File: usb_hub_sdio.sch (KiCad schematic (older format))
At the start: 26 parts, among them Q901 DMG2301L, U901 MA8627, Y901 24MHz

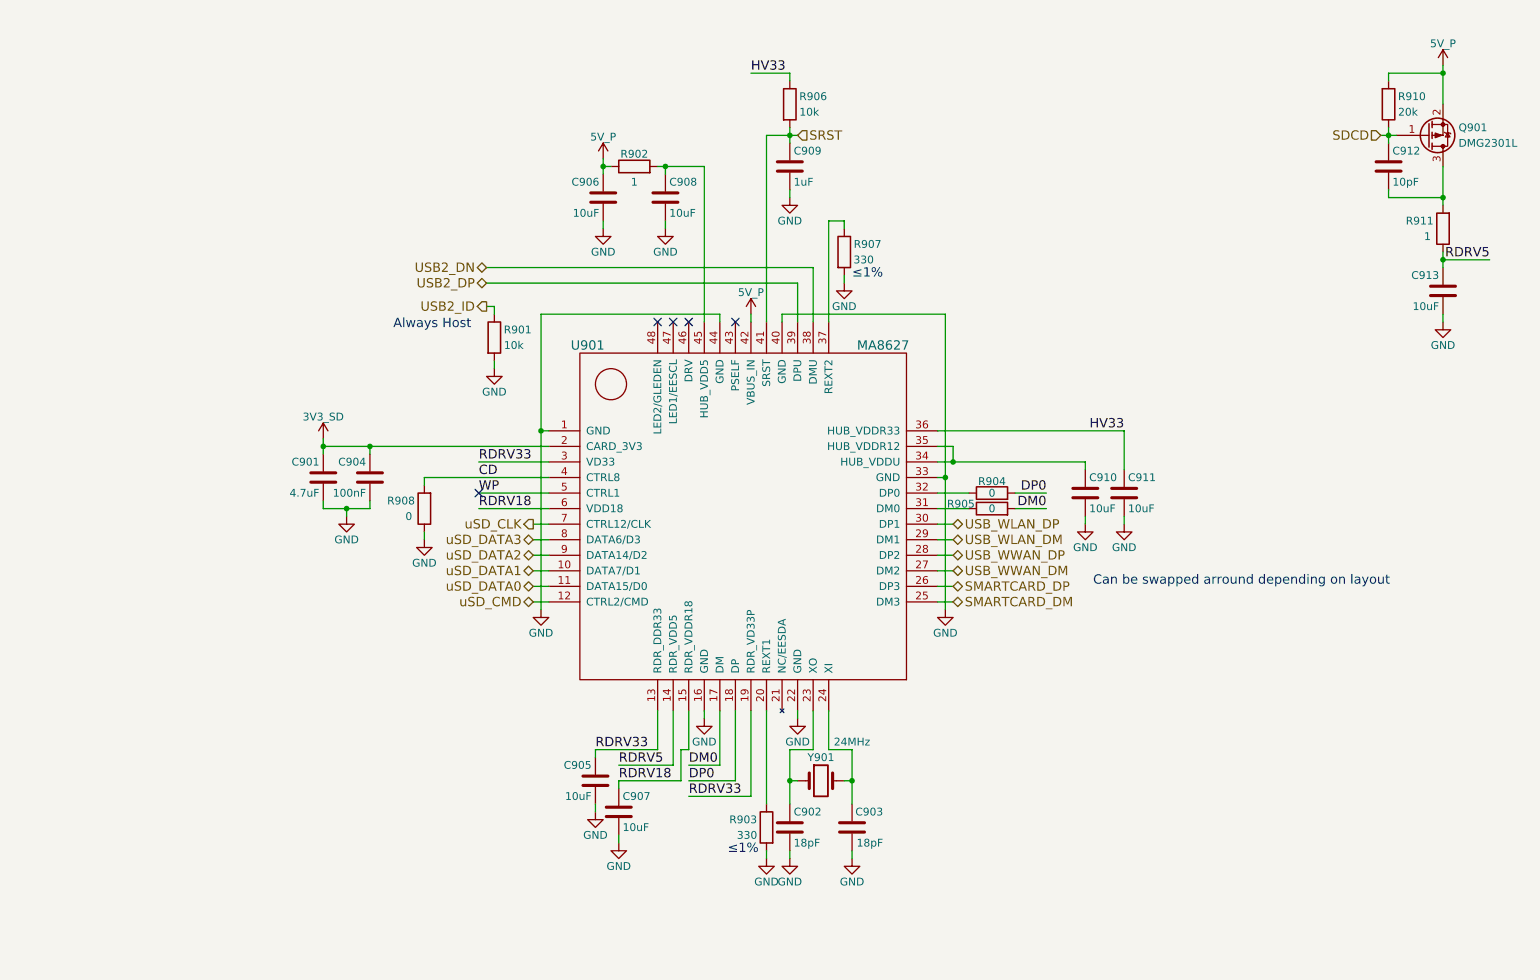
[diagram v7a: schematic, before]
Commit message: Modify the boot config/boot mode pins and switch such that only eMMC and USB (serial downloader) are boot options due to the uSD being attached to the USB<->SD bridge chip, add OV5460 notes about using the internal DVDD 1.5V regulator
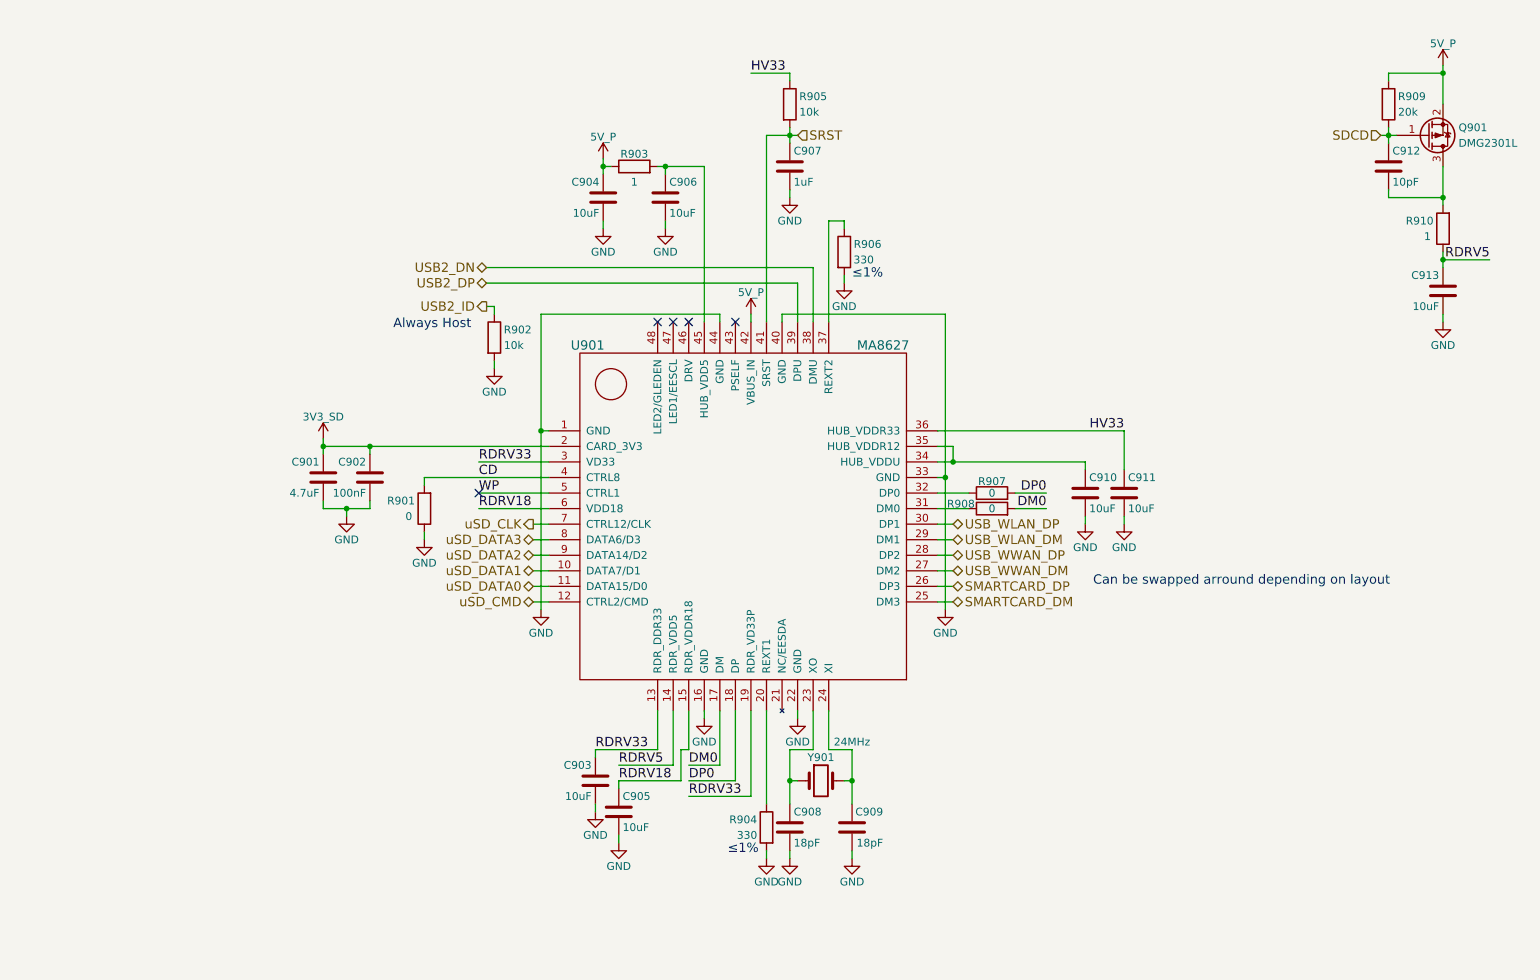
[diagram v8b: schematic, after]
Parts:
- renumbered C904 to C902, C905 to C903, C906 to C904, C907 to C905, C908 to C906, C909 to C907, C902 to C908, C903 to C909, R908 to R901, R901 to R902, R902 to R903, R903 to R904, R906 to R905, R907 to R906, R904 to R907, R905 to R908, R910 to R909, R911 to R910
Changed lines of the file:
@@
 $EndDescr
 $Comp
-L GND #PWR0138
+L GND #PWR0132
 U 1 1 5AFD409A
 P 6100 6050
-F 0 "#PWR0138" H 6100 5800 50  0001 C CNN
+F 0 "#PWR0132" H 6100 5800 50  0001 C CNN
 F 1 "GND" H 6100 5900 50  0000 C CNN
 F 2 "" H 6100 6050 50  0001 C CNN
@@
 $EndComp
 $Comp
-L GND #PWR0139
+L GND #PWR0133
 U 1 1 5AFD422F
 P 6500 6050
-F 0 "#PWR0139" H 6500 5800 50  0001 C CNN
+F 0 "#PWR0133" H 6500 5800 50  0001 C CNN
 F 1 "GND" H 6500 5900 50  0000 C CNN
 F 2 "" H 6500 6050 50  0001 C CNN
@@
 $EndComp
 $Comp
-L C C902
+L C C908
 U 1 1 5AFD532B
 P 6100 5850
-F 0 "C902" H 6125 5750 50  0000 L CNN
+F 0 "C908" H 6125 5750 50  0000 L CNN
 F 1 "18pF" H 6125 5950 50  0000 L CNN
 F 2 "Capacitors_SMD:C_0603" H 6138 5700 50  0001 C CNN
@@
 $EndComp
 $Comp
-L C C903
+L C C909
 U 1 1 5AFD53BF
 P 6500 5850
-F 0 "C903" H 6300 5750 50  0000 L CNN
+F 0 "C909" H 6300 5750 50  0000 L CNN
 F 1 "18pF" H 6300 5950 50  0000 L CNN
 F 2 "Capacitors_SMD:C_0603" H 6538 5700 50  0001 C CNN
@@
 USB2_ID
 $Comp
-L GND #PWR0140
+L GND #PWR0134
 U 1 1 5AF52101
 P 4200 2900
-F 0 "#PWR0140" H 4200 2650 50  0001 C CNN
+F 0 "#PWR0134" H 4200 2650 50  0001 C CNN
 F 1 "GND" H 4200 2750 50  0000 C CNN
 F 2 "" H 4200 2900 50  0001 C CNN
@@
 uSD_DATA3
 $Comp
-L R R901
+L R R902
 U 1 1 5B31F267
 P 4200 2700
-F 0 "R901" H 4350 2750 50  0000 C CNN
+F 0 "R902" H 4350 2750 50  0000 C CNN
 F 1 "10k" H 4325 2650 50  0000 C CNN
 F 2 "Resistors_SMD:R_0603" V 4130 2700 50  0001 C CNN
@@
 $EndComp
 $Comp
-L GND #PWR0141
+L GND #PWR0135
 U 1 1 5B07B0B9
 P 6150 5150
-F 0 "#PWR0141" H 6150 4900 50  0001 C CNN
+F 0 "#PWR0135" H 6150 4900 50  0001 C CNN
 F 1 "GND" H 6150 5000 50  0000 C CNN
 F 2 "" H 6150 5150 50  0001 C CNN
@@
 $EndComp
 $Comp
-L GND #PWR0142
+L GND #PWR0136
 U 1 1 5B07B125
 P 5550 5150
-F 0 "#PWR0142" H 5550 4900 50  0001 C CNN
+F 0 "#PWR0136" H 5550 4900 50  0001 C CNN
 F 1 "GND" H 5550 5000 50  0000 C CNN
 F 2 "" H 5550 5150 50  0001 C CNN
@@
 $EndComp
 $Comp
-L GND #PWR0143
+L GND #PWR0137
 U 1 1 5B07B2AA
 P 7100 4450
-F 0 "#PWR0143" H 7100 4200 50  0001 C CNN
+F 0 "#PWR0137" H 7100 4200 50  0001 C CNN
 F 1 "GND" H 7100 4300 50  0000 C CNN
 F 2 "" H 7100 4450 50  0001 C CNN
@@
 $EndComp
 $Comp
-L GND #PWR0144
+L GND #PWR0138
 U 1 1 5B07B66F
 P 4500 4450
-F 0 "#PWR0144" H 4500 4200 50  0001 C CNN
+F 0 "#PWR0138" H 4500 4200 50  0001 C CNN
 F 1 "GND" H 4500 4300 50  0000 C CNN
 F 2 "" H 4500 4450 50  0001 C CNN
@@
 $EndComp
 $Comp
-L R R904
+L R R907
 U 1 1 5B07D9A0
 P 7400 3700
-F 0 "R904" V 7475 3700 50  0000 C CNN
+F 0 "R907" V 7475 3700 50  0000 C CNN
 F 1 "0" V 7400 3700 50  0000 C CNN
 F 2 "Resistors_SMD:R_0603" V 7330 3700 50  0001 C CNN
@@
 $EndComp
 $Comp
-L R R905
+L R R908
 U 1 1 5B07DA80
 P 7400 3800
-F 0 "R905" V 7430 4000 50  0000 C CNN
+F 0 "R908" V 7430 4000 50  0000 C CNN
 F 1 "0" V 7400 3800 50  0000 C CNN
 F 2 "Resistors_SMD:R_0603" V 7330 3800 50  0001 C CNN
@@
 Can be swapped arround depending on layout
 $Comp
-L R R908
+L R R901
 U 1 1 5B09B6A4
 P 3750 3800
-F 0 "R908" H 3900 3750 50  0000 C CNN
+F 0 "R901" H 3900 3750 50  0000 C CNN
 F 1 "0" H 3850 3850 50  0000 C CNN
 F 2 "Resistors_SMD:R_0603" V 3680 3800 50  0001 C CNN
@@
 $EndComp
 $Comp
-L R R910
+L R R909
 U 1 1 5B09C779
 P 9950 1200
-F 0 "R910" H 10100 1150 50  0000 C CNN
+F 0 "R909" H 10100 1150 50  0000 C CNN
 F 1 "20k" H 10075 1250 50  0000 C CNN
 F 2 "Resistors_SMD:R_0603" V 9880 1200 50  0001 C CNN
@@
 $EndComp
 $Comp
-L 5V_P #PWR0145
+L 5V_P #PWR0139
 U 1 1 5B09CA5D
 P 10300 950
-F 0 "#PWR0145" H 10300 800 50  0001 C CNN
+F 0 "#PWR0139" H 10300 800 50  0001 C CNN
 F 1 "5V_P" H 10300 1090 50  0000 C CNN
 F 2 "" H 10300 950 50  0001 C CNN
@@
 $EndComp
 $Comp
-L R R911
+L R R910
 U 1 1 5B0B14ED
 P 10300 2000
-F 0 "R911" H 10450 1950 50  0000 C CNN
+F 0 "R910" H 10450 1950 50  0000 C CNN
 F 1 "1" H 10400 2050 50  0000 C CNN
 F 2 "Resistors_SMD:R_0603" V 10230 2000 50  0001 C CNN
@@
 $EndComp
 $Comp
-L GND #PWR0146
+L GND #PWR0140
 U 1 1 5B0B1862
 P 10300 2600
-F 0 "#PWR0146" H 10300 2350 50  0001 C CNN
+F 0 "#PWR0140" H 10300 2350 50  0001 C CNN
 F 1 "GND" H 10300 2450 50  0000 C CNN
 F 2 "" H 10300 2600 50  0001 C CNN
@@
 RDRV5
 $Comp
-L GND #PWR0147
+L GND #PWR0141
 U 1 1 5B0B5C77
 P 3750 4000
-F 0 "#PWR0147" H 3750 3750 50  0001 C CNN
+F 0 "#PWR0141" H 3750 3750 50  0001 C CNN
 F 1 "GND" H 3750 3850 50  0000 C CNN
 F 2 "" H 3750 4000 50  0001 C CNN
@@
 SRST
 $Comp
-L C C909
+L C C907
 U 1 1 5B0FBA1F
 P 6100 1600
-F 0 "C909" H 6125 1700 50  0000 L CNN
+F 0 "C907" H 6125 1700 50  0000 L CNN
 F 1 "1uF" H 6125 1500 50  0000 L CNN
 F 2 "Capacitors_SMD:C_0603" H 6138 1450 50  0001 C CNN
@@
 $EndComp
 $Comp
-L GND #PWR0148
+L GND #PWR0142
 U 1 1 5B0FBCD9
 P 6100 1800
-F 0 "#PWR0148" H 6100 1550 50  0001 C CNN
+F 0 "#PWR0142" H 6100 1550 50  0001 C CNN
 F 1 "GND" H 6100 1650 50  0000 C CNN
 F 2 "" H 6100 1800 50  0001 C CNN
@@
 $EndComp
 $Comp
-L R R906
+L R R905
 U 1 1 5B0FC98F
 P 6100 1200
-F 0 "R906" H 6250 1250 50  0000 C CNN
+F 0 "R905" H 6250 1250 50  0000 C CNN
 F 1 "10k" H 6225 1150 50  0000 C CNN
 F 2 "" V 6030 1200 50  0001 C CNN
@@
 HV33
 $Comp
-L GND #PWR0149
+L GND #PWR0143
 U 1 1 5B0FF7C5
 P 6450 2350
-F 0 "#PWR0149" H 6450 2100 50  0001 C CNN
+F 0 "#PWR0143" H 6450 2100 50  0001 C CNN
 F 1 "GND" H 6450 2200 50  0000 C CNN
 F 2 "" H 6450 2350 50  0001 C CNN
@@
 $EndComp
 $Comp
-L R R903
+L R R904
 U 1 1 5B101B57
 P 5950 5850
-F 0 "R903" H 6100 5900 50  0000 C CNN
+F 0 "R904" H 6100 5900 50  0000 C CNN
 F 1 "330" H 6075 5800 50  0000 C CNN
 F 2 "Resistors_SMD:R_0603" V 5880 5850 50  0001 C CNN
@@
 $EndComp
 $Comp
-L GND #PWR0150
+L GND #PWR0144
 U 1 1 5B101B5E
 P 5950 6050
-F 0 "#PWR0150" H 5950 5800 50  0001 C CNN
+F 0 "#PWR0144" H 5950 5800 50  0001 C CNN
 F 1 "GND" H 5950 5900 50  0000 C CNN
 F 2 "" H 5950 6050 50  0001 C CNN
@@
 RDRV33
 $Comp
-L GND #PWR0151
+L GND #PWR0145
 U 1 1 5B104C14
 P 8000 3900
-F 0 "#PWR0151" H 8000 3650 50  0001 C CNN
+F 0 "#PWR0145" H 8000 3650 50  0001 C CNN
 F 1 "GND" H 8000 3750 50  0000 C CNN
 F 2 "" H 8000 3900 50  0001 C CNN
@@
 $EndComp
 $Comp
-L GND #PWR0152
+L GND #PWR0146
 U 1 1 5B1079D0
 P 8250 3900
-F 0 "#PWR0152" H 8250 3650 50  0001 C CNN
+F 0 "#PWR0146" H 8250 3650 50  0001 C CNN
 F 1 "GND" H 8250 3750 50  0000 C CNN
 F 2 "" H 8250 3900 50  0001 C CNN
@@
 HV33
 $Comp
-L R R907
+L R R906
 U 1 1 5B10A19C
 P 6450 2150
-F 0 "R907" H 6600 2200 50  0000 C CNN
+F 0 "R906" H 6600 2200 50  0000 C CNN
 F 1 "330" H 6575 2100 50  0000 C CNN
 F 2 "Resistors_SMD:R_0603" V 6380 2150 50  0001 C CNN
@@
 $EndComp
 $Comp
-L C C904
+L C C902
 U 1 1 5B10DFD5
 P 3400 3600
-F 0 "C904" H 3425 3700 50  0000 L CNN
+F 0 "C902" H 3425 3700 50  0000 L CNN
 F 1 "100nF" H 3425 3500 50  0000 L CNN
 F 2 "" H 3438 3450 50  0001 C CNN
@@
 $EndComp
 $Comp
-L GND #PWR0153
+L GND #PWR0147
 U 1 1 5B10E3EB
 P 3250 3850
-F 0 "#PWR0153" H 3250 3600 50  0001 C CNN
+F 0 "#PWR0147" H 3250 3600 50  0001 C CNN
 F 1 "GND" H 3250 3700 50  0000 C CNN
 F 2 "" H 3250 3850 50  0001 C CNN
@@
 $EndComp
 $Comp
-L 3V3_SD #PWR0154
+L 3V3_SD #PWR0148
 U 1 1 5B10EE23
 P 3100 3350
-F 0 "#PWR0154" H 3100 3200 50  0001 C CNN
+F 0 "#PWR0148" H 3100 3200 50  0001 C CNN
 F 1 "3V3_SD" H 3100 3490 50  0000 C CNN
 F 2 "" H 3100 3350 50  0001 C CNN
@@
 RDRV33
 $Comp
-L C C905
+L C C903
 U 1 1 5B112B02
 P 4850 5550
-F 0 "C905" H 4875 5650 50  0000 L CNN
+F 0 "C903" H 4875 5650 50  0000 L CNN
 F 1 "10uF" H 4875 5450 50  0000 L CNN
 F 2 "Resistors_SMD:R_0603" H 4888 5400 50  0001 C CNN
@@
 $EndComp
 $Comp
-L GND #PWR0155
+L GND #PWR0149
 U 1 1 5B112BA0
 P 4850 5750
-F 0 "#PWR0155" H 4850 5500 50  0001 C CNN
+F 0 "#PWR0149" H 4850 5500 50  0001 C CNN
 F 1 "GND" H 4850 5600 50  0000 C CNN
 F 2 "" H 4850 5750 50  0001 C CNN
@@
 RDRV18
 $Comp
-L GND #PWR0156
+L GND #PWR0150
 U 1 1 5B11D61C
 P 5000 5950
-F 0 "#PWR0156" H 5000 5700 50  0001 C CNN
+F 0 "#PWR0150" H 5000 5700 50  0001 C CNN
 F 1 "GND" H 5000 5800 50  0000 C CNN
 F 2 "" H 5000 5950 50  0001 C CNN
@@
 NoConn ~ 4100 3700
 $Comp
-L 5V_P #PWR0157
+L 5V_P #PWR0151
 U 1 1 5B169FFA
 P 4900 1550
-F 0 "#PWR0157" H 4900 1400 50  0001 C CNN
+F 0 "#PWR0151" H 4900 1400 50  0001 C CNN
 F 1 "5V_P" H 4900 1690 50  0000 C CNN
 F 2 "" H 4900 1550 50  0001 C CNN
@@
 $EndComp
 $Comp
-L R R902
+L R R903
 U 1 1 5B16A0C3
 P 5100 1600
-F 0 "R902" V 5180 1600 50  0000 C CNN
+F 0 "R903" V 5180 1600 50  0000 C CNN
 F 1 "1" V 5000 1600 50  0000 C CNN
 F 2 "Resistors_SMD:R_0603" V 5030 1600 50  0001 C CNN
@@
 $EndComp
 $Comp
-L GND #PWR0158
+L GND #PWR0152
 U 1 1 5B16A294
 P 5300 2000
-F 0 "#PWR0158" H 5300 1750 50  0001 C CNN
+F 0 "#PWR0152" H 5300 1750 50  0001 C CNN
 F 1 "GND" H 5300 1850 50  0000 C CNN
 F 2 "" H 5300 2000 50  0001 C CNN
@@
 $EndComp
 $Comp
-L GND #PWR0159
+L GND #PWR0153
 U 1 1 5B16A2F7
 P 4900 2000
-F 0 "#PWR0159" H 4900 1750 50  0001 C CNN
+F 0 "#PWR0153" H 4900 1750 50  0001 C CNN
 F 1 "GND" H 4900 1850 50  0000 C CNN
 F 2 "" H 4900 2000 50  0001 C CNN
@@
 $EndComp
 $Comp
-L C C907
+L C C905
 U 1 1 5B16A93D
 P 5000 5750
-F 0 "C907" H 5025 5850 50  0000 L CNN
+F 0 "C905" H 5025 5850 50  0000 L CNN
 F 1 "10uF" H 5025 5650 50  0000 L CNN
 F 2 "Resistors_SMD:R_0603" H 5038 5600 50  0001 C CNN
@@
 $EndComp
 $Comp
-L C C908
+L C C906
 U 1 1 5B16A9CA
 P 5300 1800
-F 0 "C908" H 5325 1900 50  0000 L CNN
+F 0 "C906" H 5325 1900 50  0000 L CNN
 F 1 "10uF" H 5325 1700 50  0000 L CNN
 F 2 "Resistors_SMD:R_0603" H 5338 1650 50  0001 C CNN
@@
 $EndComp
 $Comp
-L C C906
+L C C904
 U 1 1 5B16AE2A
 P 4900 1800
-F 0 "C906" H 4925 1900 50  0000 L CNN
+F 0 "C904" H 4925 1900 50  0000 L CNN
 F 1 "10uF" H 4925 1700 50  0000 L CNN
 F 2 "Resistors_SMD:R_0603" H 4938 1650 50  0001 C CNN
@@
 $EndComp
 $Comp
-L 5V_P #PWR0160
+L 5V_P #PWR0154
 U 1 1 5B16E4EF
 P 5850 2550
-F 0 "#PWR0160" H 5850 2400 50  0001 C CNN
+F 0 "#PWR0154" H 5850 2400 50  0001 C CNN
 F 1 "5V_P" H 5850 2690 50  0000 C CNN
 F 2 "" H 5850 2550 50  0001 C CNN
